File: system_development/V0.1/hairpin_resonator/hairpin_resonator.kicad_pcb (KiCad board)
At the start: 2 copper layers, 25 x 33.5 mm, 4 parts

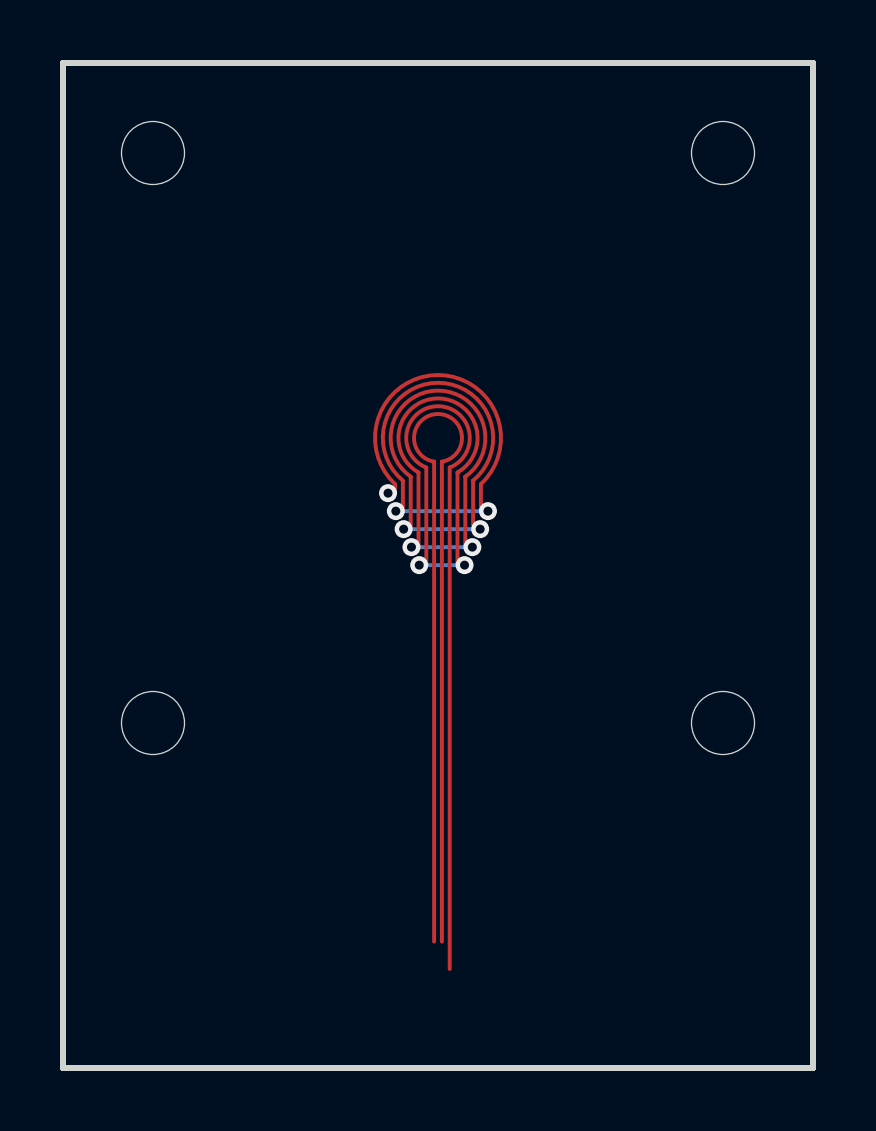
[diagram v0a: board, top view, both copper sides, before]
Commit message: updated hairpin dimensions
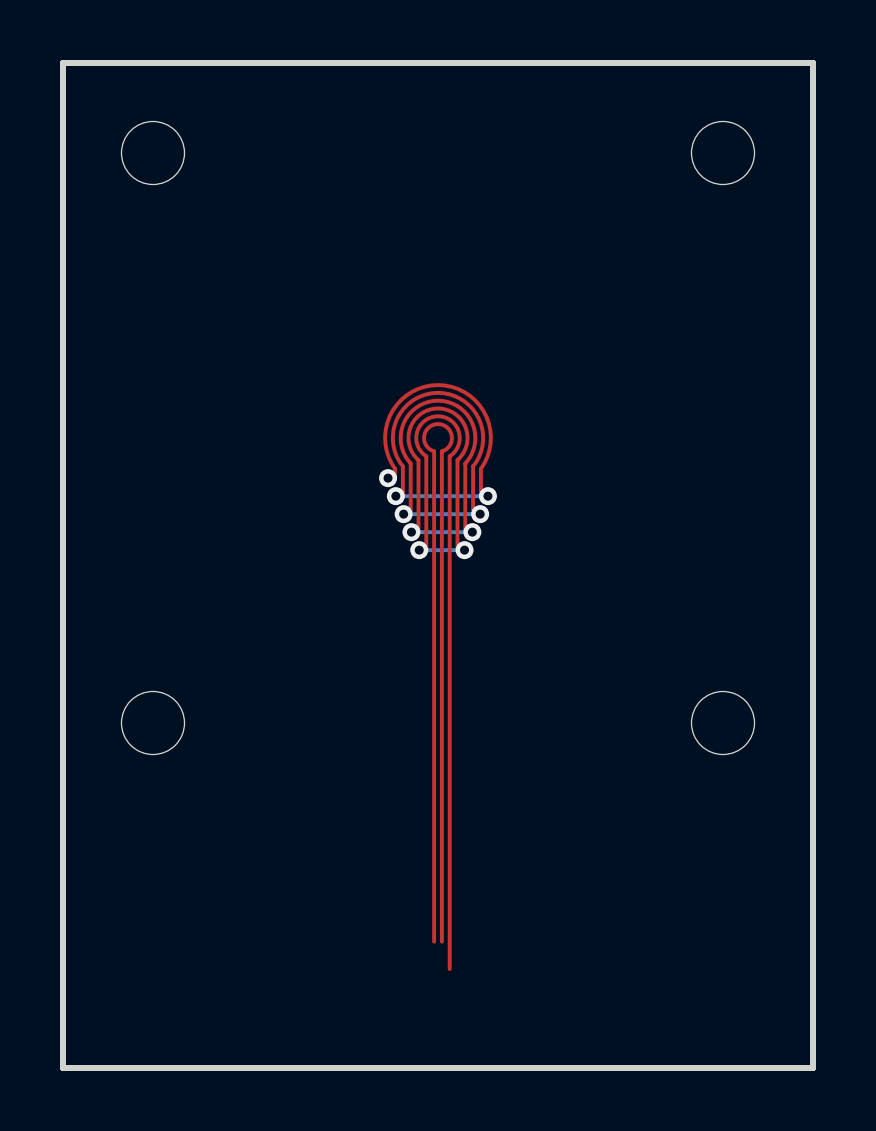
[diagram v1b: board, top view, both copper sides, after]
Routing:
- net (no net): track 74.6 -> 75.2 mm
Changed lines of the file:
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@@
 	)
 	(gr_arc
-		(start 112.11 63.4856)
-		(mid 112.5 61.44)
-		(end 112.89 63.4856)
-		(stroke
-			(width 0.13)
-			(type solid)
-		)
-		(layer "F.Cu")
-	)
-	(gr_arc
-		(start 111.59 63.79)
-		(mid 112.5 60.92)
-		(end 113.41 63.79)
-		(stroke
-			(width 0.13)
-			(type solid)
-		)
-		(layer "F.Cu")
-	)
-	(gr_arc
-		(start 112.37 63.289)
-		(mid 112.5 61.7)
-		(end 112.63 63.289)
-		(stroke
-			(width 0.13)
-			(type solid)
-		)
-		(layer "F.Cu")
-	)
-	(gr_arc
-		(start 111.07 64.038)
-		(mid 112.5 60.4)
-		(end 113.93 64.038)
-		(stroke
-			(width 0.13)
-			(type solid)
-		)
-		(layer "F.Cu")
-	)
-	(gr_arc
-		(start 111.85 63.649)
-		(mid 112.5 61.18)
-		(end 113.15 63.649)
-		(stroke
-			(width 0.13)
-			(type solid)
-		)
-		(layer "F.Cu")
-	)
-	(gr_arc
-		(start 111.33 63.92)
-		(mid 112.5 60.66)
-		(end 113.67 63.92)
+		(start 112.11 63.11)
+		(mid 112.5 61.775)
+		(end 112.89 63.11)
+		(stroke
+			(width 0.13)
+			(type solid)
+		)
+		(layer "F.Cu")
+	)
+	(gr_arc
+		(start 111.59 63.35)
+		(mid 112.5 61.255)
+		(end 113.41 63.35)
+		(stroke
+			(width 0.13)
+			(type solid)
+		)
+		(layer "F.Cu")
+	)
+	(gr_arc
+		(start 112.37 62.946)
+		(mid 112.5 62.035001)
+		(end 112.63 62.946)
+		(stroke
+			(width 0.13)
+			(type solid)
+		)
+		(layer "F.Cu")
+	)
+	(gr_arc
+		(start 111.07 63.53)
+		(mid 112.5 60.735)
+		(end 113.93 63.53)
+		(stroke
+			(width 0.13)
+			(type solid)
+		)
+		(layer "F.Cu")
+	)
+	(gr_arc
+		(start 111.85 63.24)
+		(mid 112.5 61.515)
+		(end 113.15 63.24)
+		(stroke
+			(width 0.13)
+			(type solid)
+		)
+		(layer "F.Cu")
+	)
+	(gr_arc
+		(start 111.33 63.45)
+		(mid 112.5 60.995)
+		(end 113.67 63.45)
 		(stroke
 			(width 0.13)
@@
 	)
 	(segment
-		(start 112.11 66.738)
-		(end 112.11 63.4856)
-		(width 0.13)
-		(layer "F.Cu")
-		(net 0)
-	)
-	(segment
-		(start 113.15 63.649)
-		(end 113.15 66.738)
-		(width 0.13)
-		(layer "F.Cu")
-		(net 0)
-	)
-	(segment
-		(start 113.93 64.038)
-		(end 113.93 64.938)
-		(width 0.13)
-		(layer "F.Cu")
-		(net 0)
-	)
-	(segment
-		(start 111.85 63.649)
-		(end 111.85 66.138)
-		(width 0.13)
-		(layer "F.Cu")
-		(net 0)
-	)
-	(segment
-		(start 112.63 79.289)
-		(end 112.63 63.289)
-		(width 0.13)
-		(layer "F.Cu")
-		(net 0)
-	)
-	(segment
-		(start 111.07 64.038)
-		(end 111.07 64.338)
-		(width 0.13)
-		(layer "F.Cu")
-		(net 0)
-	)
-	(segment
-		(start 111.33 63.938)
-		(end 111.33 64.938)
-		(width 0.13)
-		(layer "F.Cu")
-		(net 0)
-	)
-	(segment
-		(start 111.59 63.79)
-		(end 111.59 65.538)
-		(width 0.13)
-		(layer "F.Cu")
-		(net 0)
-	)
-	(segment
-		(start 113.41 63.79)
-		(end 113.41 66.138)
-		(width 0.13)
-		(layer "F.Cu")
-		(net 0)
-	)
-	(segment
-		(start 113.67 63.92)
-		(end 113.67 65.538)
-		(width 0.13)
-		(layer "F.Cu")
-		(net 0)
-	)
-	(segment
-		(start 112.37 79.289)
-		(end 112.37 63.289)
+		(start 112.11 66.238)
+		(end 112.11 63.11)
+		(width 0.13)
+		(layer "F.Cu")
+		(net 0)
+	)
+	(segment
+		(start 113.15 63.24)
+		(end 113.15 66.238)
+		(width 0.13)
+		(layer "F.Cu")
+		(net 0)
+	)
+	(segment
+		(start 113.93 63.53)
+		(end 113.93 64.438)
+		(width 0.13)
+		(layer "F.Cu")
+		(net 0)
+	)
+	(segment
+		(start 111.85 63.24)
+		(end 111.85 65.638)
+		(width 0.13)
+		(layer "F.Cu")
+		(net 0)
+	)
+	(segment
+		(start 112.63 62.946)
+		(end 112.63 79.289)
+		(width 0.13)
+		(layer "F.Cu")
+		(net 0)
+	)
+	(segment
+		(start 111.07 63.53)
+		(end 111.07 63.838)
+		(width 0.13)
+		(layer "F.Cu")
+		(net 0)
+	)
+	(segment
+		(start 111.33 63.45)
+		(end 111.33 64.438)
+		(width 0.13)
+		(layer "F.Cu")
+		(net 0)
+	)
+	(segment
+		(start 111.59 63.35)
+		(end 111.59 65.038)
+		(width 0.13)
+		(layer "F.Cu")
+		(net 0)
+	)
+	(segment
+		(start 113.41 63.35)
+		(end 113.41 65.638)
+		(width 0.13)
+		(layer "F.Cu")
+		(net 0)
+	)
+	(segment
+		(start 113.67 63.45)
+		(end 113.67 65.038)
+		(width 0.13)
+		(layer "F.Cu")
+		(net 0)
+	)
+	(segment
+		(start 112.37 62.946)
+		(end 112.37 79.289)
 		(width 0.13)
 		(layer "F.Cu")
@@
 	(segment
 		(start 112.89 80.2)
-		(end 112.89 63.4856)
-		(width 0.13)
-		(layer "F.Cu")
-		(net 0)
-	)
-	(via
-		(at 110.835 64.338)
-		(size 0.6)
-		(drill 0.3)
-		(layers "F.Cu" "B.Cu")
-		(net 0)
-	)
-	(via
-		(at 111.095 64.938)
-		(size 0.6)
-		(drill 0.3)
-		(layers "F.Cu" "B.Cu")
-		(net 0)
-	)
-	(via
-		(at 111.355 65.538)
-		(size 0.6)
-		(drill 0.3)
-		(layers "F.Cu" "B.Cu")
-		(net 0)
-	)
-	(via
-		(at 113.645 66.138)
-		(size 0.6)
-		(drill 0.3)
-		(layers "F.Cu" "B.Cu")
-		(net 0)
-	)
-	(via
-		(at 111.615 66.138)
-		(size 0.6)
-		(drill 0.3)
-		(layers "F.Cu" "B.Cu")
-		(net 0)
-	)
-	(via
-		(at 113.385 66.738)
-		(size 0.6)
-		(drill 0.3)
-		(layers "F.Cu" "B.Cu")
-		(net 0)
-	)
-	(via
-		(at 111.875 66.738)
-		(size 0.6)
-		(drill 0.3)
-		(layers "F.Cu" "B.Cu")
-		(net 0)
-	)
-	(via
-		(at 113.905 65.538)
-		(size 0.6)
-		(drill 0.3)
-		(layers "F.Cu" "B.Cu")
-		(net 0)
-	)
-	(via
-		(at 114.165 64.938)
-		(size 0.6)
-		(drill 0.3)
-		(layers "F.Cu" "B.Cu")
-		(net 0)
-	)
-	(segment
-		(start 111.615 66.138)
-		(end 113.645 66.138)
-		(width 0.13)
-		(layer "B.Cu")
-		(net 0)
-	)
-	(segment
-		(start 113.905 65.538)
-		(end 111.355 65.538)
-		(width 0.13)
-		(layer "B.Cu")
-		(net 0)
-	)
-	(segment
-		(start 111.095 64.938)
-		(end 114.165 64.938)
-		(width 0.13)
-		(layer "B.Cu")
-		(net 0)
-	)
-	(segment
-		(start 113.385 66.738)
-		(end 111.875 66.738)
-		(width 0.13)
-		(layer "B.Cu")
+		(end 112.89 63.11)
+		(width 0.13)
+		(layer "F.Cu")
+		(net 0)
+	)
+	(via
+		(at 110.835 63.838)
+		(size 0.6)
+		(drill 0.3)
+		(layers "F.Cu" "B.Cu")
+		(net 0)
+	)
+	(via
+		(at 111.095 64.438)
+		(size 0.6)
+		(drill 0.3)
+		(layers "F.Cu" "B.Cu")
+		(net 0)
+	)
+	(via
+		(at 111.355 65.038)
+		(size 0.6)
+		(drill 0.3)
+		(layers "F.Cu" "B.Cu")
+		(net 0)
+	)
+	(via
+		(at 113.645 65.638)
+		(size 0.6)
+		(drill 0.3)
+		(layers "F.Cu" "B.Cu")
+		(net 0)
+	)
+	(via
+		(at 111.615 65.638)
+		(size 0.6)
+		(drill 0.3)
+		(layers "F.Cu" "B.Cu")
+		(net 0)
+	)
+	(via
+		(at 113.385 66.238)
+		(size 0.6)
+		(drill 0.3)
+		(layers "F.Cu" "B.Cu")
+		(net 0)
+	)
+	(via
+		(at 111.875 66.238)
+		(size 0.6)
+		(drill 0.3)
+		(layers "F.Cu" "B.Cu")
+		(net 0)
+	)
+	(via
+		(at 113.905 65.038)
+		(size 0.6)
+		(drill 0.3)
+		(layers "F.Cu" "B.Cu")
+		(net 0)
+	)
+	(via
+		(at 114.165 64.438)
+		(size 0.6)
+		(drill 0.3)
+		(layers "F.Cu" "B.Cu")
+		(net 0)
+	)
+	(segment
+		(start 113.905 65.038)
+		(end 111.355 65.038)
+		(width 0.13)
+		(layer "B.Cu")
+		(net 0)
+	)
+	(segment
+		(start 111.095 64.438)
+		(end 114.165 64.438)
+		(width 0.13)
+		(layer "B.Cu")
+		(net 0)
+	)
+	(segment
+		(start 113.385 66.238)
+		(end 111.875 66.238)
+		(width 0.13)
+		(layer "B.Cu")
+		(net 0)
+	)
+	(segment
+		(start 111.615 65.638)
+		(end 113.645 65.638)
+		(width 0.13)
+		(layer "B.Cu")
